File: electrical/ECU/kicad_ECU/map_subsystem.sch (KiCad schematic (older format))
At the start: 5 parts

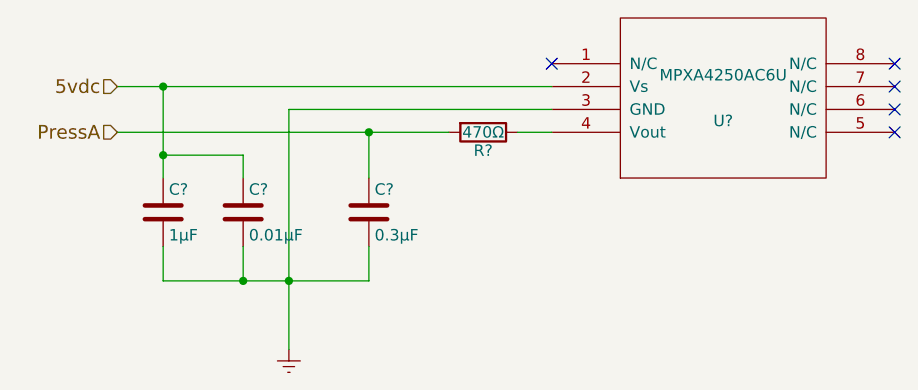
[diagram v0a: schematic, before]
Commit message: fixed some naming errors and initial round of double checking
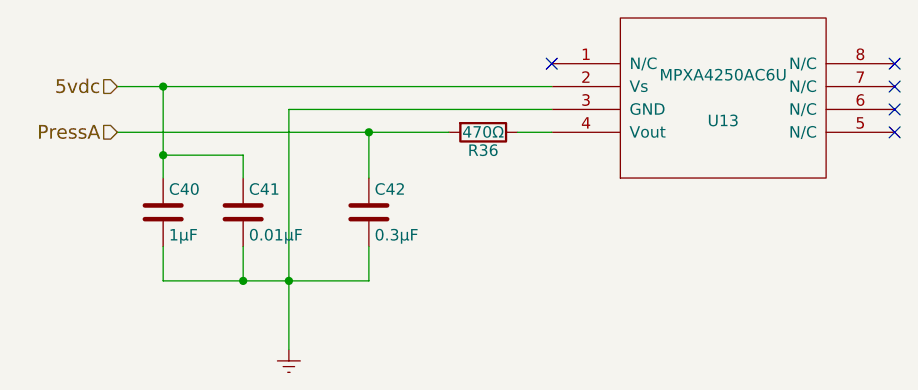
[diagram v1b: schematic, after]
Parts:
- gave numbers to parts that had none: 5
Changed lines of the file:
@@
 $Descr A4 11693 8268
 encoding utf-8
-Sheet 14 33
+Sheet 18 33
 Title "Manifold Absolute Pressure"
 Date ""
@@
 $EndDescr
 $Comp
-L MPXA4250AC6U U?
+L MPXA4250AC6U U12
 U 1 1 5921F130
 P 6150 3100
-AR Path="/5974D512/59776310/5921F130" Ref="U?"  Part="1"
-AR Path="/5974D512/5977631A/5921F130" Ref="U?"  Part="1"
-F 0 "U?" H 6150 3000 50  0000 C CNN
+AR Path="/5974D512/59776310/5921F130" Ref="U12"  Part="1"
+AR Path="/5974D512/5977631A/5921F130" Ref="U13"  Part="1"
+F 0 "U13" H 6150 3000 50  0000 C CNN
 F 1 "MPXA4250AC6U" H 6150 3200 50  0000 C CNN
 F 2 "MODULE" H 6150 3100 50  0001 C CNN
@@
 5vdc
 $Comp
-L Earth #PWR?
+L Earth #PWR45
 U 1 1 5929DA6E
 P 4250 4200
-AR Path="/5974D512/59776310/5929DA6E" Ref="#PWR?"  Part="1"
-AR Path="/5974D512/5977631A/5929DA6E" Ref="#PWR?"  Part="1"
-F 0 "#PWR?" H 4250 3950 50  0001 C CNN
+AR Path="/5974D512/59776310/5929DA6E" Ref="#PWR45"  Part="1"
+AR Path="/5974D512/5977631A/5929DA6E" Ref="#PWR46"  Part="1"
+F 0 "#PWR46" H 4250 3950 50  0001 C CNN
 F 1 "Earth" H 4250 4050 50  0001 C CNN
 F 2 "" H 4250 4200 50  0001 C CNN
@@
 PressA
 $Comp
-L R R?
+L R R35
 U 1 1 5929DB00
 P 5100 3250
-AR Path="/5974D512/59776310/5929DB00" Ref="R?"  Part="1"
-AR Path="/5974D512/5977631A/5929DB00" Ref="R?"  Part="1"
-F 0 "R?" V 5180 3250 50  0000 C CNN
+AR Path="/5974D512/59776310/5929DB00" Ref="R35"  Part="1"
+AR Path="/5974D512/5977631A/5929DB00" Ref="R36"  Part="1"
+F 0 "R36" V 5180 3250 50  0000 C CNN
 F 1 "470Ω" V 5100 3250 50  0000 C CNN
 F 2 "" V 5030 3250 50  0001 C CNN
@@
 	3500 3050 5400 3050
 $Comp
-L C C?
+L C C39
 U 1 1 5929DF2C
 P 4600 3600
-AR Path="/5974D512/59776310/5929DF2C" Ref="C?"  Part="1"
-AR Path="/5974D512/5977631A/5929DF2C" Ref="C?"  Part="1"
-F 0 "C?" H 4625 3700 50  0000 L CNN
+AR Path="/5974D512/59776310/5929DF2C" Ref="C39"  Part="1"
+AR Path="/5974D512/5977631A/5929DF2C" Ref="C42"  Part="1"
+F 0 "C42" H 4625 3700 50  0000 L CNN
 F 1 "0.3μF" H 4625 3500 50  0000 L CNN
 F 2 "" H 4638 3450 50  0001 C CNN
@@
 Connection ~ 4600 3250
 $Comp
-L C C?
+L C C38
 U 1 1 5929DFD9
 P 4050 3600
-AR Path="/5974D512/59776310/5929DFD9" Ref="C?"  Part="1"
-AR Path="/5974D512/5977631A/5929DFD9" Ref="C?"  Part="1"
-F 0 "C?" H 4075 3700 50  0000 L CNN
+AR Path="/5974D512/59776310/5929DFD9" Ref="C38"  Part="1"
+AR Path="/5974D512/5977631A/5929DFD9" Ref="C41"  Part="1"
+F 0 "C41" H 4075 3700 50  0000 L CNN
 F 1 "0.01μF" H 4075 3500 50  0000 L CNN
 F 2 "" H 4088 3450 50  0001 C CNN
@@
 $EndComp
 $Comp
-L C C?
+L C C37
 U 1 1 5929DFF8
 P 3700 3600
-AR Path="/5974D512/59776310/5929DFF8" Ref="C?"  Part="1"
-AR Path="/5974D512/5977631A/5929DFF8" Ref="C?"  Part="1"
-F 0 "C?" H 3725 3700 50  0000 L CNN
+AR Path="/5974D512/59776310/5929DFF8" Ref="C37"  Part="1"
+AR Path="/5974D512/5977631A/5929DFF8" Ref="C40"  Part="1"
+F 0 "C40" H 3725 3700 50  0000 L CNN
 F 1 "1μF" H 3725 3500 50  0000 L CNN
 F 2 "" H 3738 3450 50  0001 C CNN
